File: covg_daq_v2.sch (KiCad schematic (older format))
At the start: 5 parts, among them J3 HDMI_A

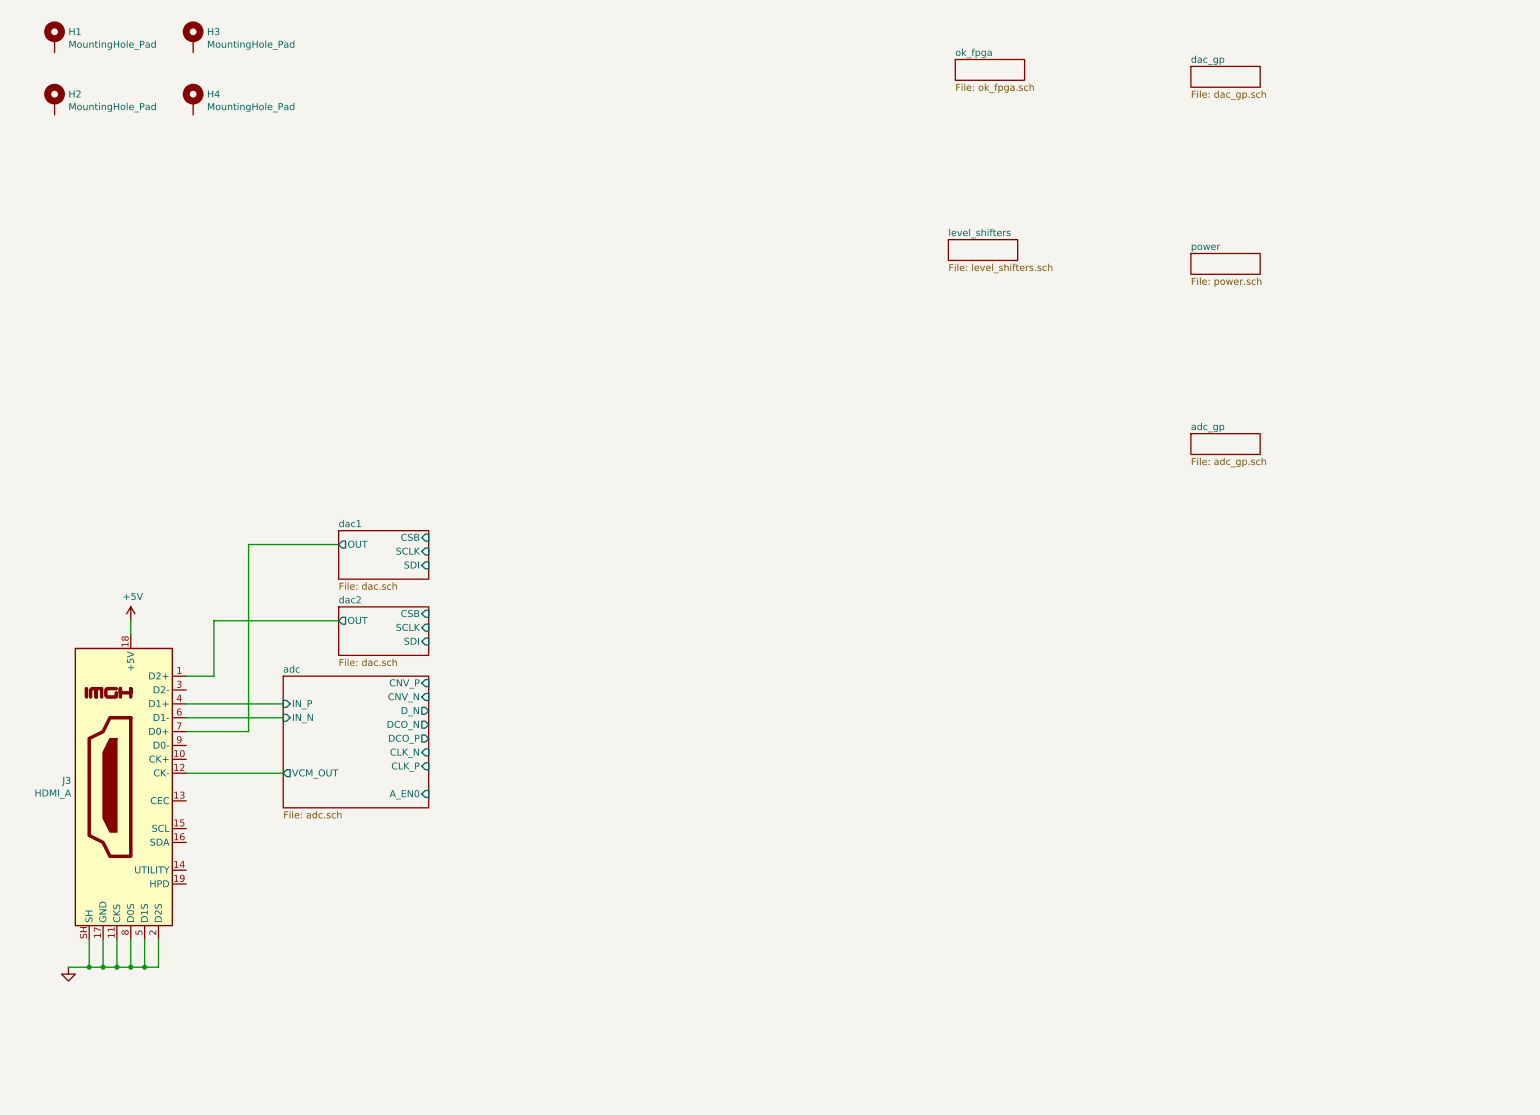
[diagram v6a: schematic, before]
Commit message: modify LVDS connections for AD7960
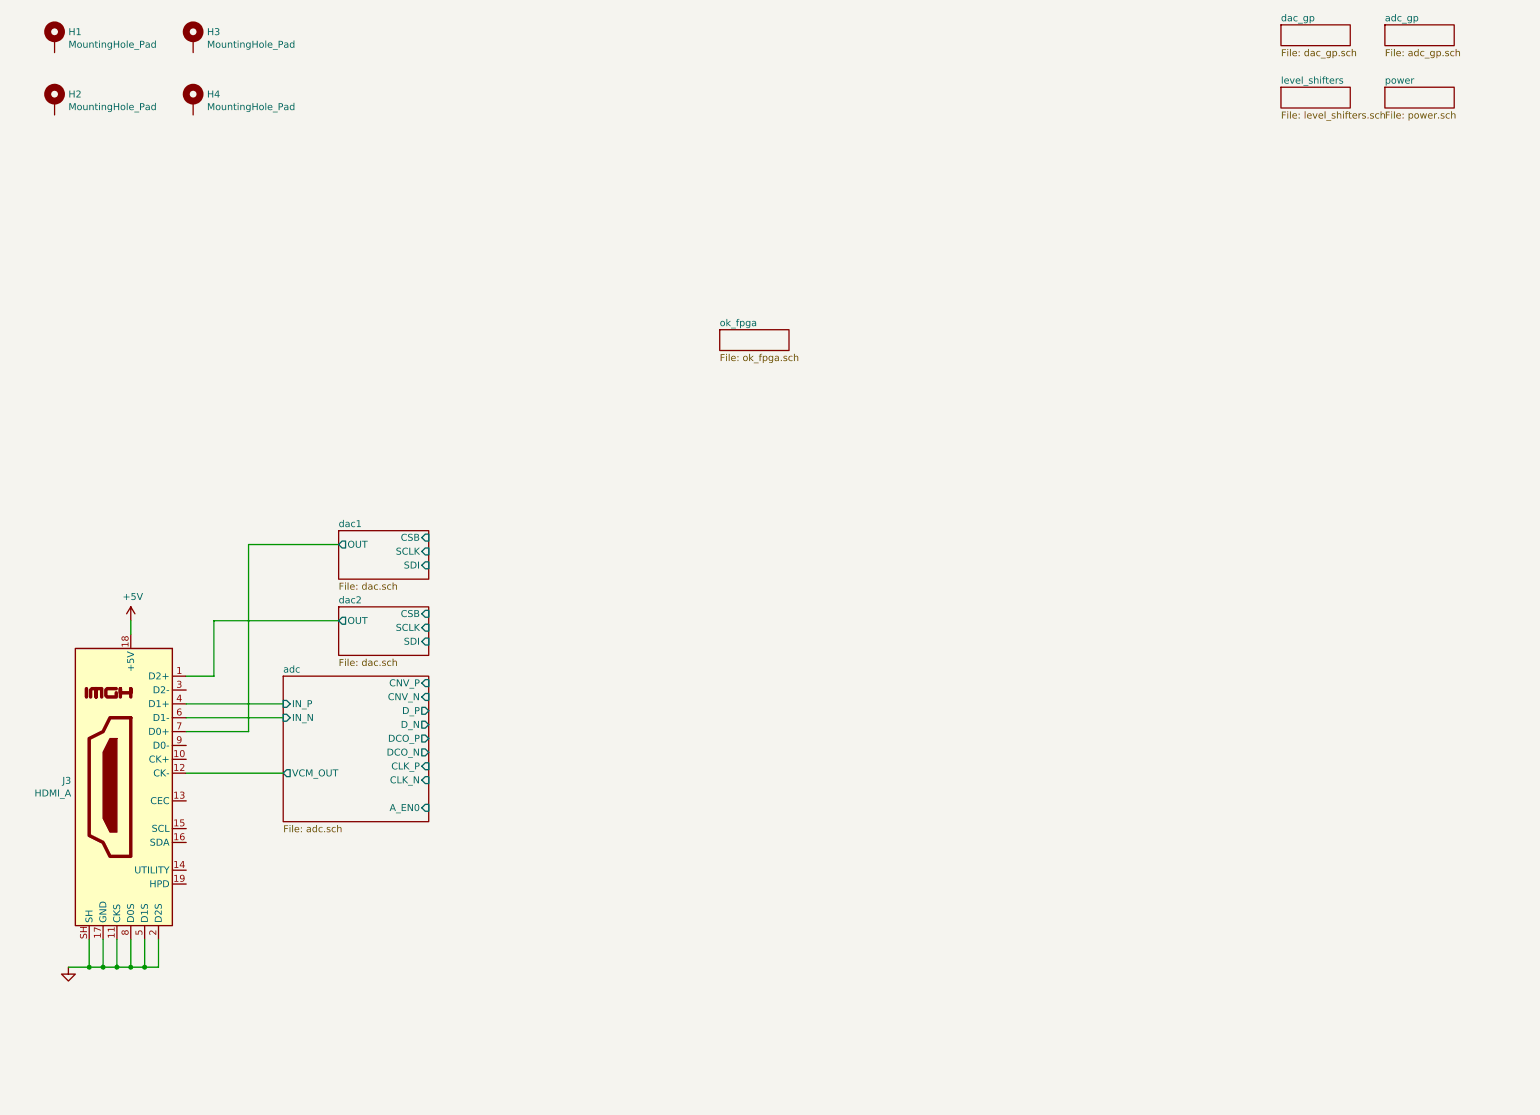
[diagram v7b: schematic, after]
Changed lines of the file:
@@
 $EndDescr
 $Sheet
-S 7150 2200 500  150
+S 9550 1100 500  150
 U 6095A38A
 F0 "level_shifters" 50
@@
 $EndSheet
 $Sheet
-S 8900 950  500  150
+S 9550 650  500  150
 U 6095BD4C
 F0 "dac_gp" 50
@@
 $EndSheet
 $Sheet
-S 8900 2300 500  150
+S 10300 1100 500  150
 U 6095BE10
 F0 "power" 50
@@
 $EndSheet
 $Sheet
-S 7200 900  500  150
+S 5500 2850 500  150
 U 6095A302
 F0 "ok_fpga" 50
@@
 	1050 7450 1150 7450
 $Sheet
-S 2350 5350 1050 950
+S 2350 5350 1050 1050
 U 6095A697
 F0 "adc" 50
@@
 F2 "CNV_P" I R 3400 5400 50
 F3 "CNV_N" I R 3400 5500 50
-F4 "D_N" O R 3400 5600 50
-F5 "DCO_N" O R 3400 5700 50
+F4 "D_N" O R 3400 5700 50
+F5 "DCO_N" O R 3400 5900 50
 F6 "DCO_P" O R 3400 5800 50
-F7 "CLK_N" I R 3400 5900 50
+F7 "CLK_N" I R 3400 6100 50
 F8 "CLK_P" I R 3400 6000 50
 F9 "VCM_OUT" O L 2350 6050 50
 F10 "IN_N" I L 2350 5650 50
 F11 "IN_P" I L 2350 5550 50
-F12 "A_EN0" I R 3400 6200 50
+F12 "A_EN0" I R 3400 6300 50
+F13 "D_P" O R 3400 5600 50
 $EndSheet
 $Sheet
@@
 $EndComp
 $Sheet
-S 8900 3600 500  150
+S 10300 650  500  150
 U 6095A004
 F0 "adc_gp" 50

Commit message: moved level shifters to FPGA
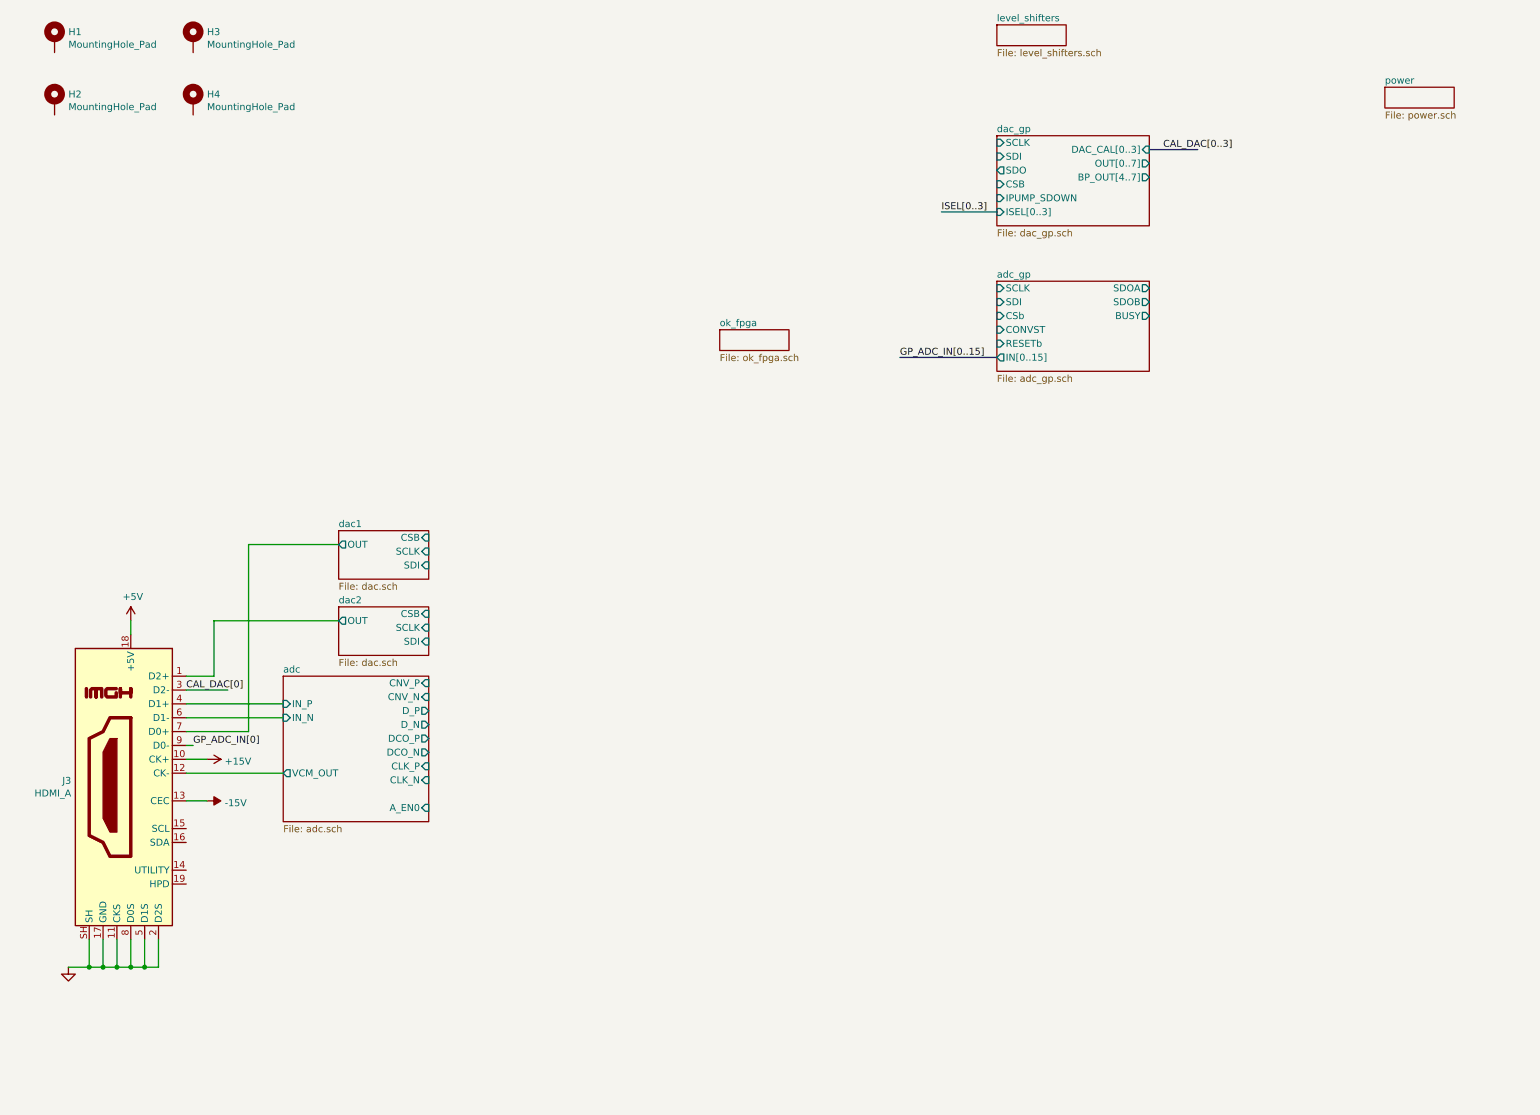
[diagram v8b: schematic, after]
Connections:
- net labels added: +15V, -15V, CAL_DAC[0..3], CAL_DAC[0], GP_ADC_IN[0..15], GP_ADC_IN[0], ISEL[0..3]
- wire segments 22 -> 26
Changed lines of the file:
@@
 $EndDescr
 $Sheet
-S 9550 1100 500  150
+S 7500 650  500  150
 U 6095A38A
 F0 "level_shifters" 50
@@
 $EndSheet
 $Sheet
-S 9550 650  500  150
+S 7500 1450 1100 650
 U 6095BD4C
 F0 "dac_gp" 50
 F1 "dac_gp.sch" 50
+F2 "SCLK" I L 7500 1500 50
+F3 "SDI" I L 7500 1600 50
+F4 "SDO" O L 7500 1700 50
+F5 "CSB" I L 7500 1800 50
+F6 "IPUMP_SDOWN" I L 7500 1900 50
+F7 "DAC_CAL[0..3]" I R 8600 1550 50
+F8 "ISEL[0..3]" I L 7500 2000 50
+F9 "OUT[0..7]" O R 8600 1650 50
+F10 "BP_OUT[4..7]" O R 8600 1750 50
 $EndSheet
 $Sheet
@@
 $EndComp
 $Sheet
-S 10300 650  500  150
+S 7500 2500 1100 650
 U 6095A004
 F0 "adc_gp" 50
 F1 "adc_gp.sch" 50
+F2 "SCLK" I L 7500 2550 50
+F3 "BUSY" O R 8600 2750 50
+F4 "CONVST" I L 7500 2850 50
+F5 "SDOA" O R 8600 2550 50
+F6 "SDOB" O R 8600 2650 50
+F7 "CSb" I L 7500 2750 50
+F8 "SDI" I L 7500 2650 50
+F9 "RESETb" I L 7500 2950 50
+F10 "IN[0..15]" O L 7500 3050 50
 $EndSheet
 Wire Wire Line
@@
 Wire Wire Line
 	1250 4950 1250 5050
+Wire Wire Line
+	1650 5450 1950 5450
+Text Label 1650 5450 0    50   ~ 0
+CAL_DAC[0]
+Wire Bus Line
+	8600 1550 8950 1550
+Text Label 8700 1550 0    50   ~ 0
+CAL_DAC[0..3]
+Wire Bus Line
+	7500 3050 6800 3050
+Text Label 6800 3050 0    50   ~ 0
+GP_ADC_IN[0..15]
+Wire Bus Line
+	7500 2000 7100 2000
+Text Label 7100 2000 0    50   ~ 0
+ISEL[0..3]
+Text Label 1700 5850 0    50   ~ 0
+GP_ADC_IN[0]
+Wire Wire Line
+	1650 5850 1700 5850
+$Comp
+L power:+15V #PWR?
+U 1 1 619DB399
+P 1800 5950
+F 0 "#PWR?" H 1800 5800 50  0001 C CNN
+F 1 "+15V" V 1815 6078 50  0000 L CNN
+F 2 "" H 1800 5950 50  0001 C CNN
+F 3 "" H 1800 5950 50  0001 C CNN
+	1    1800 5950
+	0    1    1    0
+$EndComp
+Wire Wire Line
+	1800 5950 1650 5950
+$Comp
+L power:-15V #PWR?
+U 1 1 619DC10E
+P 1800 6250
+F 0 "#PWR?" H 1800 6350 50  0001 C CNN
+F 1 "-15V" V 1815 6378 50  0000 L CNN
+F 2 "" H 1800 6250 50  0001 C CNN
+F 3 "" H 1800 6250 50  0001 C CNN
+	1    1800 6250
+	0    1    1    0
+$EndComp
+Wire Wire Line
+	1800 6250 1650 6250
 $EndSCHEMATC
